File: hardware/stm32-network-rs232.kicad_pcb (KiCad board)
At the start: 2 copper layers, 85.2 x 47.2 mm, 57 parts, among them J1 USB, M1 Mount Hole, M2 Mount Hole, M3 Mount Hole, M4 Mount Hole, P1 BELFUSE-08B0-1X1T-06-F, P2 P10, P3 DEBUG, P4 SWD, P5 RS232-TAP, P6 RS-232-DB-9-DTE, P7 P03, P8 P03, U1 ENC28J60, U2 STM32-48PIN, U3 MAX3221, U4 MOSFET-P, U5 ZLDO1117, X1 25MHz, X2 8MHz

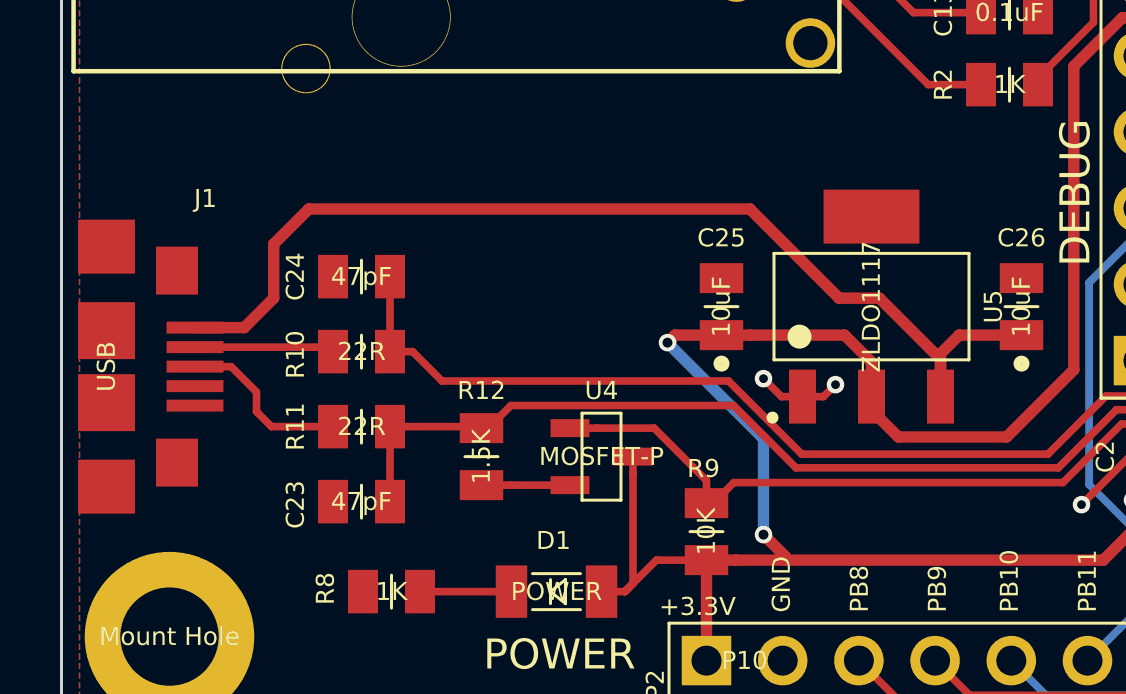
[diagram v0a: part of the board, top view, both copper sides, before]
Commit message: move usb port in a little
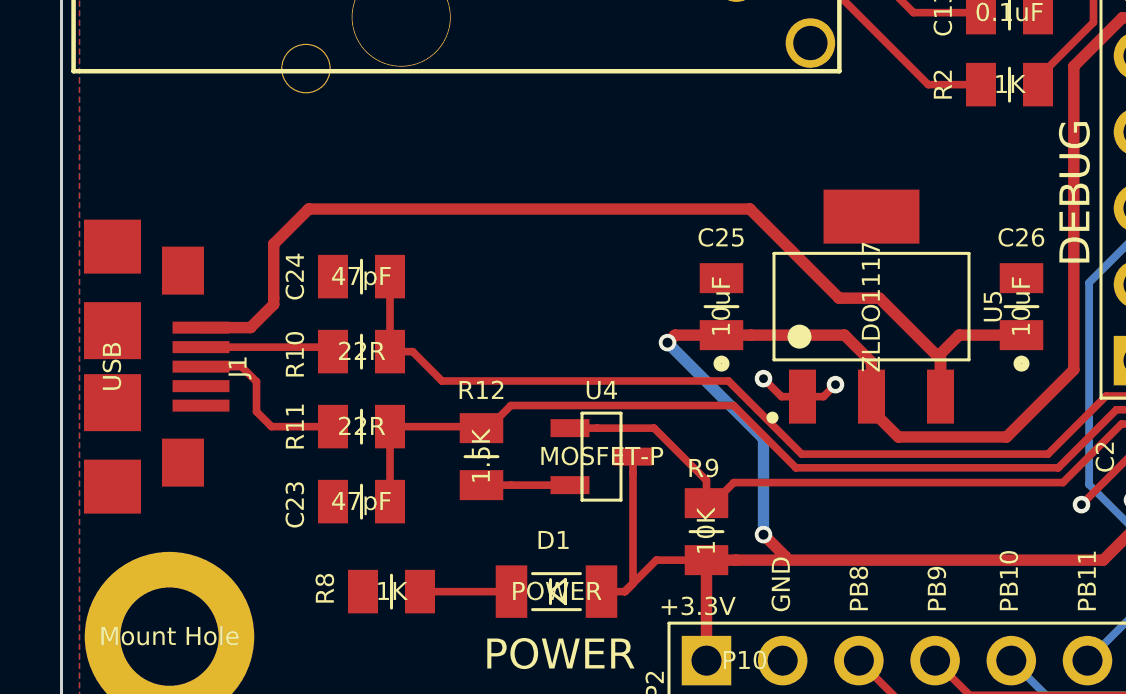
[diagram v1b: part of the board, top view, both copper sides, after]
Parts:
- moved J1 0.20 mm to (51.7, 86.0)

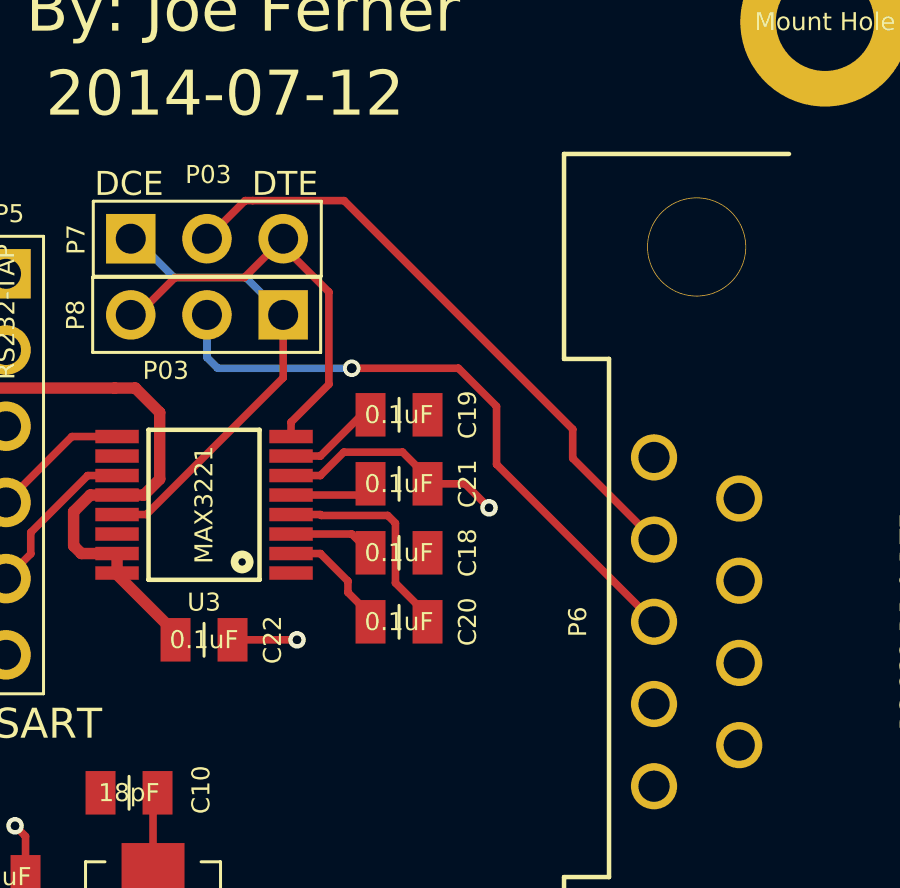
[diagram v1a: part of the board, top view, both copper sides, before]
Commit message: fix pin order on DB-9
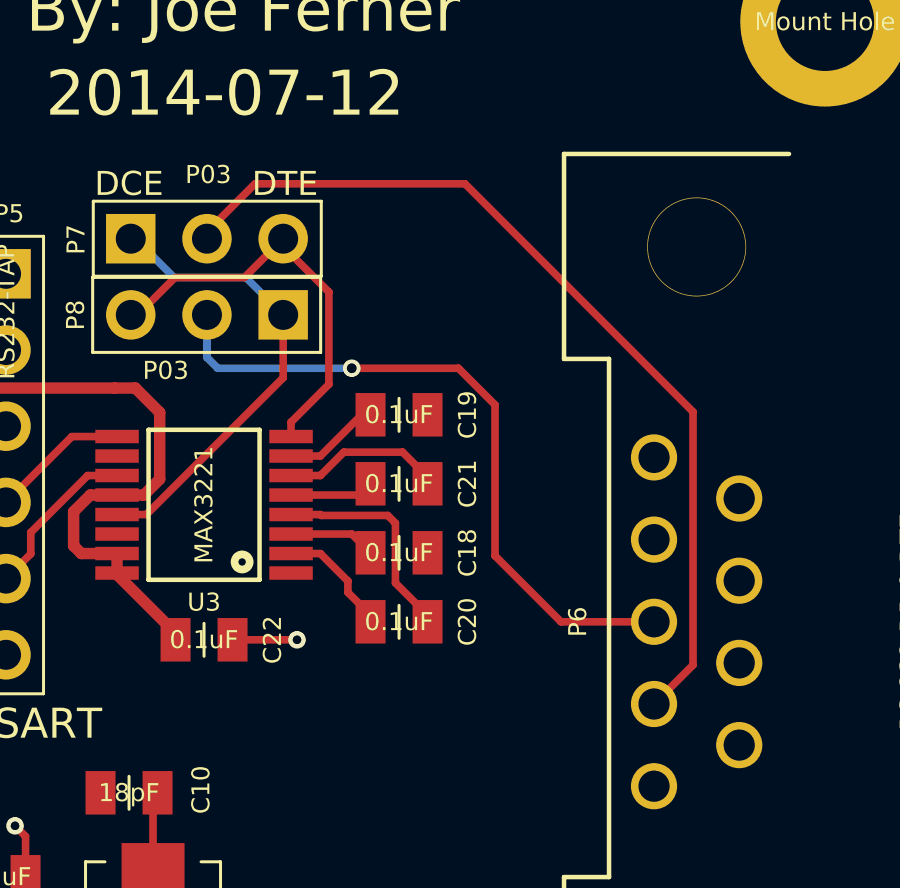
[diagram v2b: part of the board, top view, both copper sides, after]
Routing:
- net /DB9RX: track 20.7 -> 30.5 mm
- net Net-(C21-Pad2): track 7.82 -> 5.44 mm, vias 1 -> 0
- net /DB9TX: track 21.1 -> 22.9 mm
